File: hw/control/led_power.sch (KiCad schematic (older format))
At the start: 19 parts, among them U801 LM2678T-ADJ

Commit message: [hw] Minor updates in control layout
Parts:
- removed R1103: 10K, Resistor_SMD:R_0805_2012Metric_Pad1.20x1.40mm_HandSolder, symbol Device:R
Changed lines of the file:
@@
 F3 "EN" O R 3650 4000 50
 $EndSheet
-Wire Wire Line
-	4900 4000 3900 4000
 Text HLabel 2100 4000 0    50   Input ~ 0
 EN_3V3
@@
 Wire Wire Line
 	4900 2500 4900 4000
-$Comp
-L power:GND #PWR0803
-U 1 1 618AFCCB
-P 3900 4500
-AR Path="/614AB031/618AFCCB" Ref="#PWR0803"  Part="1"
-AR Path="/614AE8DA/618AFCCB" Ref="#PWR01103"  Part="1"
-AR Path="/614AB031/618915A5/618AFCCB" Ref="#PWR?"  Part="1"
-AR Path="/614AE8DA/618915A5/618AFCCB" Ref="#PWR?"  Part="1"
-F 0 "#PWR01103" H 3900 4250 50  0001 C CNN
-F 1 "GND" H 3905 4327 50  0000 C CNN
-F 2 "" H 3900 4500 50  0001 C CNN
-F 3 "" H 3900 4500 50  0001 C CNN
-	1    3900 4500
-	1    0    0    -1
-$EndComp
 Wire Wire Line
-	3900 4500 3900 4400
-Wire Wire Line
-	3900 4100 3900 4000
-Connection ~ 3900 4000
-Wire Wire Line
-	3900 4000 3650 4000
-$Comp
-L Device:R R1103
-U 1 1 618C0BB7
-P 3900 4250
-AR Path="/614AE8DA/618C0BB7" Ref="R1103"  Part="1"
-AR Path="/614AB031/618C0BB7" Ref="R803"  Part="1"
-F 0 "R1103" H 3970 4296 50  0000 L CNN
-F 1 "10K" H 3970 4205 50  0000 L CNN
-F 2 "Resistor_SMD:R_0805_2012Metric_Pad1.20x1.40mm_HandSolder" V 3830 4250 50  0001 C CNN
-F 3 "~" H 3900 4250 50  0001 C CNN
-	1    3900 4250
-	1    0    0    -1
-$EndComp
+	3650 4000 4900 4000
 $EndSCHEMATC

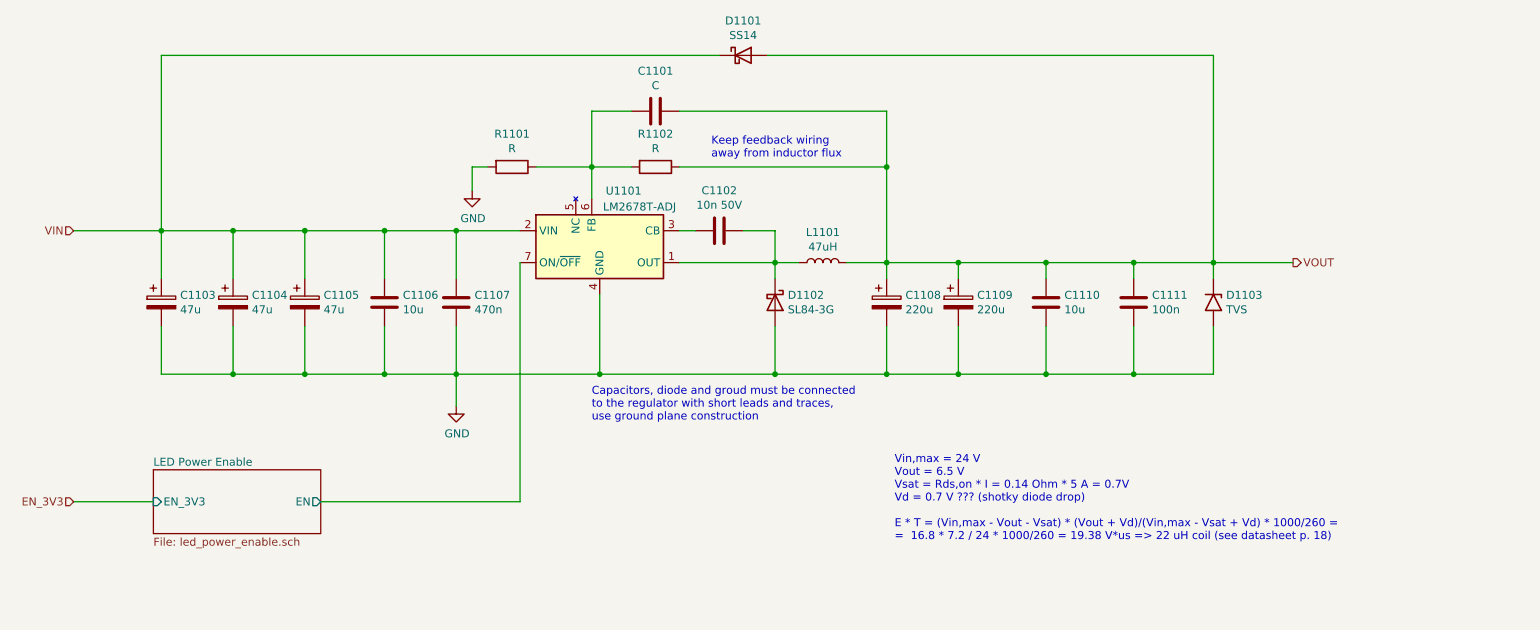
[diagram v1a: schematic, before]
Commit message: [hw] Calculate LED power supply feedback resistors
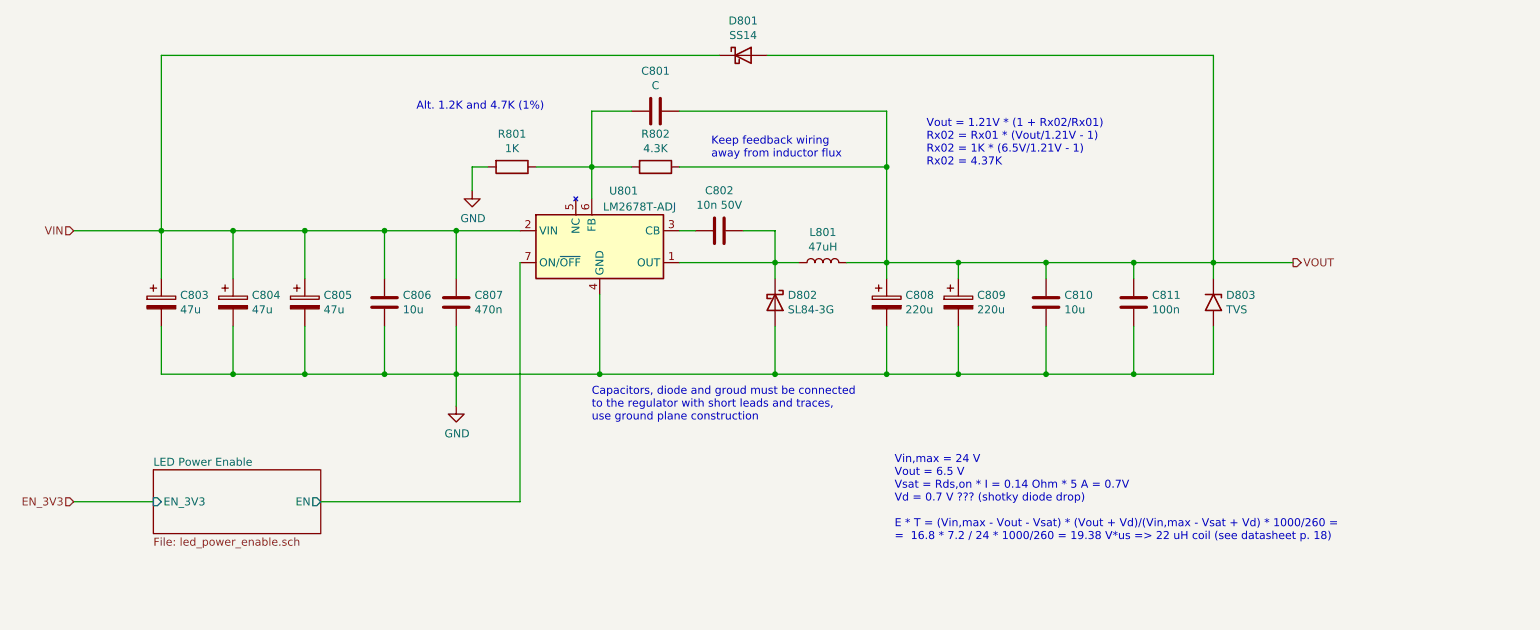
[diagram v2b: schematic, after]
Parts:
- R1101: value R -> 1K
- R1102: value R -> 4.3K
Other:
- note added: "Alt. 1.2K and 4.7K (1%)"
- note added: "Vout = 1.21V * (1 + Rx02/Rx01)\nRx02 = Rx01 * (Vout/1.21V - 1)\nRx02 = 1K * (6.5V/1.21V - 1)\nRx02 = 4.37K"
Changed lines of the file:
@@
 $Descr A4 11693 8268
 encoding utf-8
-Sheet 11 15
+Sheet 8 15
 Title "WS2812 Controller"
 Date "2021-10-10"
@@
 AR Path="/614AB031/6145ECF0" Ref="U801"  Part="1"
 AR Path="/614AE8DA/6145ECF0" Ref="U1101"  Part="1"
-F 0 "U1101" H 5550 2750 50  0000 C CNN
+F 0 "U801" H 5550 2750 50  0000 C CNN
 F 1 "LM2678T-ADJ" H 5650 2650 50  0000 C CNN
 F 2 "Package_TO_SOT_THT:TO-220-7_P2.54x3.7mm_StaggerOdd_Lead3.8mm_Vertical" H 5450 2150 50  0001 L CIN
@@
 AR Path="/614AB031/6145FC0F" Ref="C802"  Part="1"
 AR Path="/614AE8DA/6145FC0F" Ref="C1102"  Part="1"
-F 0 "C1102" V 5898 2300 50  0000 C CNN
+F 0 "C802" V 5898 2300 50  0000 C CNN
 F 1 "10n 50V" V 5989 2300 50  0000 C CNN
 F 2 "Capacitor_SMD:C_0805_2012Metric_Pad1.18x1.45mm_HandSolder" H 6188 2150 50  0001 C CNN
@@
 AR Path="/614AB031/61460B18" Ref="#PWR0802"  Part="1"
 AR Path="/614AE8DA/61460B18" Ref="#PWR01102"  Part="1"
-F 0 "#PWR01102" H 4500 3150 50  0001 C CNN
+F 0 "#PWR0802" H 4500 3150 50  0001 C CNN
 F 1 "GND" H 4505 3227 50  0000 C CNN
 F 2 "" H 4500 3400 50  0001 C CNN
@@
 AR Path="/614AE8DA/61461C6E" Ref="D1102"  Part="1"
 AR Path="/614AB031/61461C6E" Ref="D802"  Part="1"
-F 0 "D1102" V 6454 2830 50  0000 L CNN
+F 0 "D802" V 6454 2830 50  0000 L CNN
 F 1 "SL84-3G" V 6545 2830 50  0000 L CNN
 F 2 "Diode_SMD:D_SMC_Handsoldering" H 6500 2750 50  0001 C CNN
@@
 AR Path="/614AE8DA/61462D51" Ref="L1101"  Part="1"
 AR Path="/614AB031/61462D51" Ref="L801"  Part="1"
-F 0 "L1101" V 6990 2500 50  0000 C CNN
+F 0 "L801" V 6990 2500 50  0000 C CNN
 F 1 "47uH" V 6899 2500 50  0000 C CNN
 F 2 "Inductor_THT:L_Toroid_Vertical_L22.4mm_W10.2mm_P7.90mm_Vishay_TJ4" H 6800 2500 50  0001 C CNN
@@
 AR Path="/614AE8DA/61463CC3" Ref="C1108"  Part="1"
 AR Path="/614AB031/61463CC3" Ref="C808"  Part="1"
-F 0 "C1108" H 7318 2796 50  0000 L CNN
+F 0 "C808" H 7318 2796 50  0000 L CNN
 F 1 "220u" H 7318 2705 50  0000 L CNN
 F 2 "Capacitor_THT:CP_Radial_D8.0mm_P3.50mm" H 7238 2600 50  0001 C CNN
@@
 AR Path="/614AE8DA/6146511A" Ref="C1109"  Part="1"
 AR Path="/614AB031/6146511A" Ref="C809"  Part="1"
-F 0 "C1109" H 7768 2796 50  0000 L CNN
+F 0 "C809" H 7768 2796 50  0000 L CNN
 F 1 "220u" H 7768 2705 50  0000 L CNN
 F 2 "Capacitor_THT:CP_Radial_D8.0mm_P3.50mm" H 7688 2600 50  0001 C CNN
@@
 AR Path="/614AE8DA/61465477" Ref="C1105"  Part="1"
 AR Path="/614AB031/61465477" Ref="C805"  Part="1"
-F 0 "C1105" H 3668 2796 50  0000 L CNN
+F 0 "C805" H 3668 2796 50  0000 L CNN
 F 1 "47u" H 3668 2705 50  0000 L CNN
 F 2 "Capacitor_THT:CP_Radial_D8.0mm_P3.50mm" H 3588 2600 50  0001 C CNN
@@
 AR Path="/614AE8DA/614679D1" Ref="C1104"  Part="1"
 AR Path="/614AB031/614679D1" Ref="C804"  Part="1"
-F 0 "C1104" H 3218 2796 50  0000 L CNN
+F 0 "C804" H 3218 2796 50  0000 L CNN
 F 1 "47u" H 3218 2705 50  0000 L CNN
 F 2 "Capacitor_THT:CP_Radial_D8.0mm_P3.50mm" H 3138 2600 50  0001 C CNN
@@
 AR Path="/614AE8DA/61467CFC" Ref="C1103"  Part="1"
 AR Path="/614AB031/61467CFC" Ref="C803"  Part="1"
-F 0 "C1103" H 2768 2796 50  0000 L CNN
+F 0 "C803" H 2768 2796 50  0000 L CNN
 F 1 "47u" H 2768 2705 50  0000 L CNN
 F 2 "Capacitor_THT:CP_Radial_D8.0mm_P3.50mm" H 2688 2600 50  0001 C CNN
@@
 AR Path="/614AE8DA/614681BF" Ref="C1107"  Part="1"
 AR Path="/614AB031/614681BF" Ref="C807"  Part="1"
-F 0 "C1107" H 4615 2796 50  0000 L CNN
+F 0 "C807" H 4615 2796 50  0000 L CNN
 F 1 "470n" H 4615 2705 50  0000 L CNN
 F 2 "Capacitor_SMD:C_0805_2012Metric_Pad1.18x1.45mm_HandSolder" H 4538 2600 50  0001 C CNN
@@
 AR Path="/614AE8DA/6147393D" Ref="R1102"  Part="1"
 AR Path="/614AB031/6147393D" Ref="R802"  Part="1"
-F 0 "R1102" V 5543 1900 50  0000 C CNN
-F 1 "R" V 5634 1900 50  0000 C CNN
+F 0 "R802" V 5543 1900 50  0000 C CNN
+F 1 "4.3K" V 5634 1900 50  0000 C CNN
 F 2 "Resistor_SMD:R_0805_2012Metric_Pad1.20x1.40mm_HandSolder" V 5680 1900 50  0001 C CNN
 F 3 "~" H 5750 1900 50  0001 C CNN
@@
 AR Path="/614AE8DA/61475A47" Ref="R1101"  Part="1"
 AR Path="/614AB031/61475A47" Ref="R801"  Part="1"
-F 0 "R1101" V 4643 1900 50  0000 C CNN
-F 1 "R" V 4734 1900 50  0000 C CNN
+F 0 "R801" V 4643 1900 50  0000 C CNN
+F 1 "1K" V 4734 1900 50  0000 C CNN
 F 2 "Resistor_SMD:R_0805_2012Metric_Pad1.20x1.40mm_HandSolder" V 4780 1900 50  0001 C CNN
 F 3 "~" H 4850 1900 50  0001 C CNN
@@
 AR Path="/614AE8DA/61477A40" Ref="#PWR01101"  Part="1"
 AR Path="/614AB031/61477A40" Ref="#PWR0801"  Part="1"
-F 0 "#PWR01101" H 4600 1800 50  0001 C CNN
+F 0 "#PWR0801" H 4600 1800 50  0001 C CNN
 F 1 "GND" H 4605 1877 50  0000 C CNN
 F 2 "" H 4600 2050 50  0001 C CNN
@@
 AR Path="/614AB031/6169A3CC" Ref="C811"  Part="1"
 AR Path="/614AE8DA/6169A3CC" Ref="C1111"  Part="1"
-F 0 "C1111" H 8865 2796 50  0000 L CNN
+F 0 "C811" H 8865 2796 50  0000 L CNN
 F 1 "100n" H 8865 2705 50  0000 L CNN
 F 2 "Capacitor_SMD:C_0805_2012Metric_Pad1.18x1.45mm_HandSolder" H 8788 2600 50  0001 C CNN
@@
 AR Path="/614AB031/616AD78A" Ref="C801"  Part="1"
 AR Path="/614AE8DA/616AD78A" Ref="C1101"  Part="1"
-F 0 "C1101" V 5498 1550 50  0000 C CNN
+F 0 "C801" V 5498 1550 50  0000 C CNN
 F 1 "C" V 5589 1550 50  0000 C CNN
 F 2 "Capacitor_SMD:C_0805_2012Metric_Pad1.18x1.45mm_HandSolder" H 5788 1400 50  0001 C CNN
@@
 AR Path="/614AB031/616C4247" Ref="D803"  Part="1"
 AR Path="/614AE8DA/616C4247" Ref="D1103"  Part="1"
-F 0 "D1103" V 9204 2830 50  0000 L CNN
+F 0 "D803" V 9204 2830 50  0000 L CNN
 F 1 "TVS" V 9295 2830 50  0000 L CNN
 F 2 "Diode_SMD:D_SMA_Handsoldering" H 9250 2550 50  0001 C CNN
@@
 AR Path="/614AB031/617136B8" Ref="C810"  Part="1"
 AR Path="/614AE8DA/617136B8" Ref="C1110"  Part="1"
-F 0 "C1110" H 8315 2796 50  0000 L CNN
+F 0 "C810" H 8315 2796 50  0000 L CNN
 F 1 "10u" H 8315 2705 50  0000 L CNN
 F 2 "Capacitor_SMD:C_1210_3225Metric_Pad1.33x2.70mm_HandSolder" H 8238 2600 50  0001 C CNN
@@
 AR Path="/614AB031/61725C25" Ref="C806"  Part="1"
 AR Path="/614AE8DA/61725C25" Ref="C1106"  Part="1"
-F 0 "C1106" H 4165 2796 50  0000 L CNN
+F 0 "C806" H 4165 2796 50  0000 L CNN
 F 1 "10u" H 4165 2705 50  0000 L CNN
 F 2 "Capacitor_SMD:C_1210_3225Metric_Pad1.33x2.70mm_HandSolder" H 4088 2600 50  0001 C CNN
@@
 AR Path="/614AB031/616C93E8" Ref="D801"  Part="1"
 AR Path="/614AE8DA/616C93E8" Ref="D1101"  Part="1"
-F 0 "D1101" H 6300 1417 50  0000 C CNN
+F 0 "D801" H 6300 1417 50  0000 C CNN
 F 1 "SS14" H 6300 1326 50  0000 C CNN
 F 2 "Diode_SMD:D_SMA-SMB_Universal_Handsoldering" H 6300 1200 50  0001 C CNN
@@
 Wire Wire Line
 	3650 4000 4900 4000
+Text Notes 7450 1900 0    50   ~ 0
+Vout = 1.21V * (1 + Rx02/Rx01)\nRx02 = Rx01 * (Vout/1.21V - 1)\nRx02 = 1K * (6.5V/1.21V - 1)\nRx02 = 4.37K
+Text Notes 4250 1550 0    50   ~ 0
+Alt. 1.2K and 4.7K (1%)
 $EndSCHEMATC
